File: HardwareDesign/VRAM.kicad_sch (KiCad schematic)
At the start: 8 parts, among them U801 IDT7134, U802 IDT7134, U803 GAL22V10, U804 74HCT574

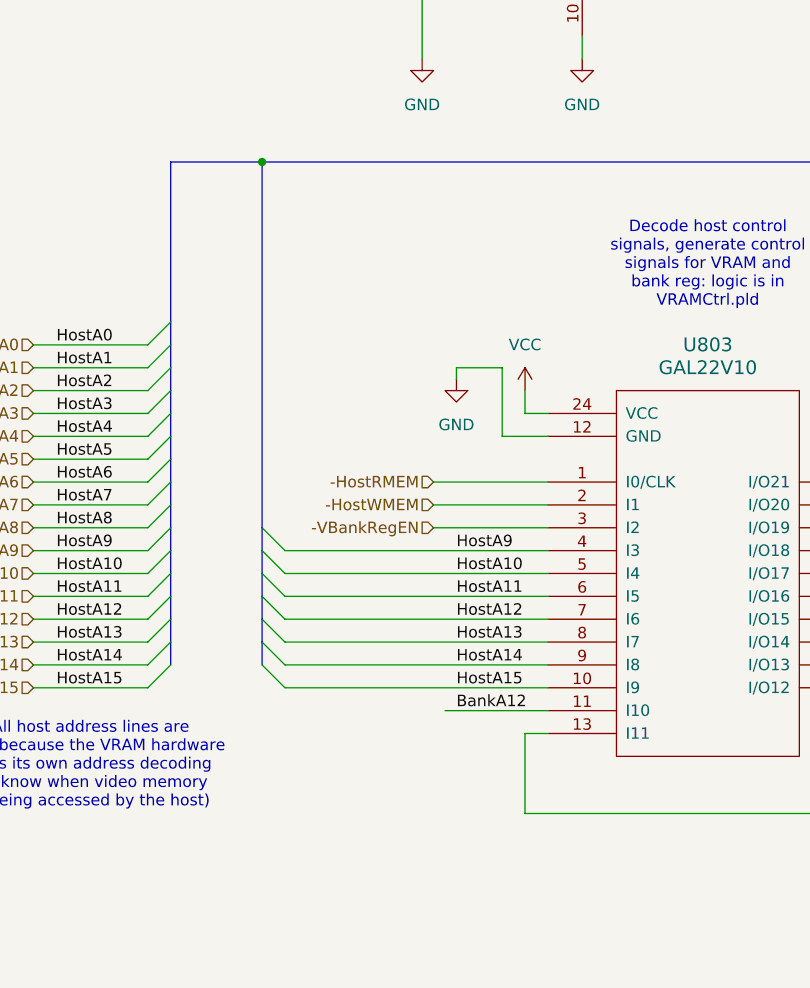
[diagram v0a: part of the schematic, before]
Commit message: VRAM control GAL doesn't need HostA9, HostA10
Only HostA11..HostA15 are needed to determine which 2KB
block of host memory is being accessed.
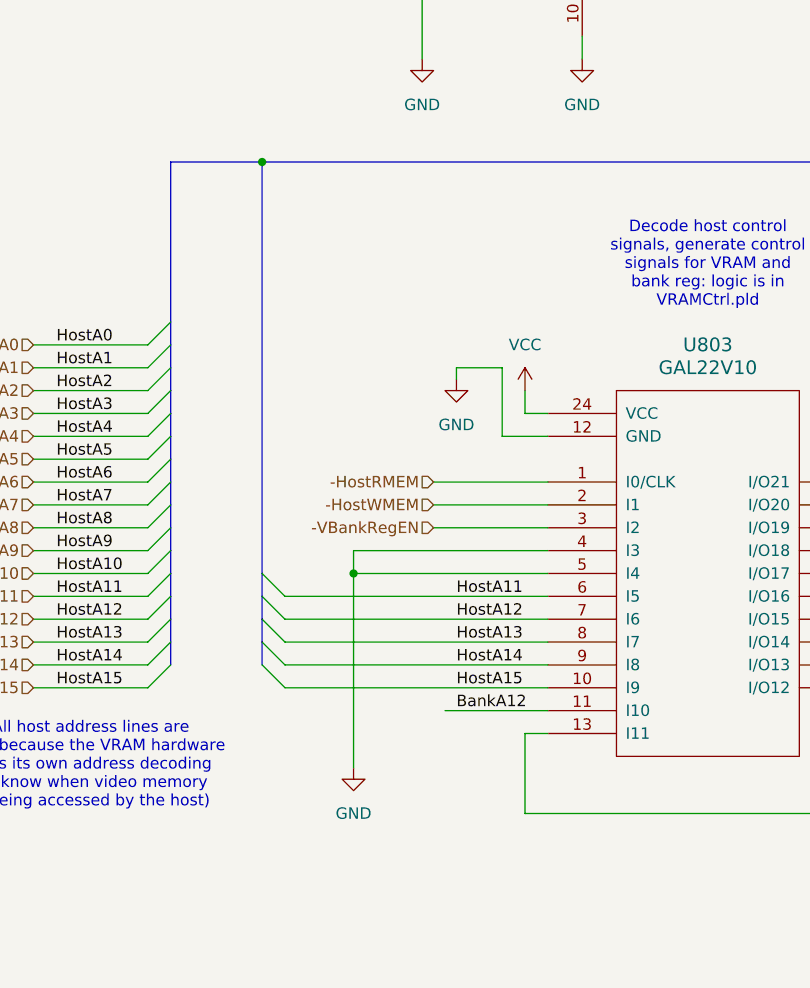
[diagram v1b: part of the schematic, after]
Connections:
- net GND: now also U803.4 (I3), U803.5 (I4)
- net HostA10: no longer U803.5 (I4)
- net HostA9: no longer U803.4 (I3)
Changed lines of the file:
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@@
 	)
 	(junction
+		(at 60.96 128.27)
+		(diameter 0)
+		(color 0 0 0 0)
+	)
+	(junction
 		(at 60.96 203.2)
 		(diameter 0)
@@
 	)
 	(bus_entry
-		(at 50.8 125.73)
-		(size 2.54 2.54)
-		(stroke
-			(width 0)
-			(type default)
-		)
-	)
-	(bus_entry
 		(at 281.94 67.31)
 		(size 2.54 -2.54)
@@
 	)
 	(bus_entry
-		(at 50.8 123.19)
-		(size 2.54 2.54)
-		(stroke
-			(width 0)
-			(type default)
-		)
-	)
-	(bus_entry
 		(at 289.56 82.55)
 		(size 2.54 -2.54)
@@
 		)
 	)
-	(bus
-		(pts
-			(xy 50.8 82.55) (xy 50.8 123.19)
-		)
-		(stroke
-			(width 0)
-			(type default)
-		)
-	)
 	(wire
 		(pts
@@
 	(wire
 		(pts
+			(xy 60.96 125.73) (xy 60.96 128.27)
+		)
+		(stroke
+			(width 0)
+			(type default)
+		)
+	)
+	(wire
+		(pts
 			(xy 242.57 41.91) (xy 242.57 25.4)
 		)
@@
 	(wire
 		(pts
+			(xy 60.96 128.27) (xy 60.96 149.86)
+		)
+		(stroke
+			(width 0)
+			(type default)
+		)
+	)
+	(wire
+		(pts
 			(xy 242.57 110.49) (xy 242.57 97.79)
 		)
@@
 	(wire
 		(pts
-			(xy 53.34 125.73) (xy 82.55 125.73)
-		)
-		(stroke
-			(width 0)
-			(type default)
-		)
-	)
-	(wire
-		(pts
 			(xy 242.57 205.74) (xy 242.57 193.04)
 		)
@@
 		)
 	)
-	(bus
+	(wire
 		(pts
-			(xy 40.64 128.27) (xy 40.64 125.73)
+			(xy 82.55 125.73) (xy 60.96 125.73)
 		)
 		(stroke
@@
 		)
 	)
-	(wire
+	(bus
 		(pts
-			(xy 118.11 128.27) (xy 139.7 128.27)
+			(xy 40.64 128.27) (xy 40.64 125.73)
 		)
 		(stroke
@@
 		)
 	)
-	(bus
+	(wire
 		(pts
-			(xy 284.48 154.94) (xy 284.48 157.48)
+			(xy 118.11 128.27) (xy 139.7 128.27)
 		)
 		(stroke
@@
 		)
 	)
-	(wire
+	(bus
 		(pts
-			(xy 53.34 128.27) (xy 82.55 128.27)
+			(xy 284.48 154.94) (xy 284.48 157.48)
 		)
 		(stroke
@@
 		)
 	)
-	(bus
-		(pts
-			(xy 50.8 123.19) (xy 50.8 125.73)
-		)
-		(stroke
-			(width 0)
-			(type default)
-		)
-	)
 	(wire
 		(pts
@@
 	(bus
 		(pts
-			(xy 50.8 125.73) (xy 50.8 128.27)
+			(xy 50.8 82.55) (xy 50.8 128.27)
 		)
 		(stroke
@@
 	(wire
 		(pts
+			(xy 60.96 128.27) (xy 82.55 128.27)
+		)
+		(stroke
+			(width 0)
+			(type default)
+		)
+	)
+	(wire
+		(pts
 			(xy 118.11 125.73) (xy 139.7 125.73)
 		)
@@
 		)
 	)
-	(label "HostA9"
-		(at 72.39 125.73 0)
-		(fields_autoplaced yes)
-		(effects
-			(font
-				(size 1.27 1.27)
-			)
-			(justify left bottom)
-		)
-	)
 	(label "ReadoutA9"
 		(at 237.49 109.22 90)
@@
 		)
 	)
-	(label "HostA10"
-		(at 72.39 128.27 0)
-		(fields_autoplaced yes)
-		(effects
-			(font
-				(size 1.27 1.27)
-			)
-			(justify left bottom)
-		)
-	)
 	(label "HostA6"
 		(at 234.95 36.83 90)
@@
 					(unit 1)
 				)
+			)
+		)
+	)
+	(symbol
+		(lib_id "power:GND")
+		(at 60.96 149.86 0)
+		(unit 1)
+		(exclude_from_sim no)
+		(in_bom yes)
+		(on_board yes)
+		(dnp no)
+		(fields_autoplaced yes)
+		(property "Reference" "#PWR070"
+			(at 60.96 156.21 0)
+			(effects
+				(font
+					(size 1.27 1.27)
+				)
+				(hide yes)
+			)
+		)
+		(property "Value" "GND"
+			(at 60.96 154.94 0)
+			(effects
+				(font
+					(size 1.27 1.27)
+				)
+			)
+		)
+		(property "Footprint" ""
+			(at 60.96 149.86 0)
+			(effects
+				(font
+					(size 1.27 1.27)
+				)
+				(hide yes)
+			)
+		)
+		(property "Datasheet" ""
+			(at 60.96 149.86 0)
+			(effects
+				(font
+					(size 1.27 1.27)
+				)
+				(hide yes)
+			)
+		)
+		(property "Description" "Power symbol creates a global label with name \"GND\" , ground"
+			(at 60.96 149.86 0)
+			(effects
+				(font
+					(size 1.27 1.27)
+				)
+				(hide yes)
+			)
+		)
+		(pin "1"
+		)
+		(instances
+			(project "HW_VGA"
+				(path "/c4bd4b39-993a-4195-805f-b4de6fa4aea5/5c8f70a9-e360-4ba4-b352-4320618fb690"
+					(reference "#PWR070")
+					(unit 1)
+				)
